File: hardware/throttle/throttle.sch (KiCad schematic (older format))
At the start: 10 parts

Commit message: Added info + revisions + date
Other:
- note added: "1.0.0"
- note added: "10/02/2021"
- note added: "Info:\nENA, IN1 and IN2 are to connect\nto the relevantly labelled pins on\nthe L298N board."
- note added: "Throttle Board"
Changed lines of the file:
@@
 Wire Wire Line
 	3400 2400 3150 2400
+Text Notes 10550 7650 0    50   ~ 0
+1.0.0
+Text Notes 8150 7650 0    50   ~ 0
+10/02/2021
+Text Notes 7350 7500 0    50   ~ 0
+Throttle Board
+Text Notes 5450 1300 0    50   ~ 0
+Info:\nENA, IN1 and IN2 are to connect\nto the relevantly labelled pins on\nthe L298N board.
 $EndSCHEMATC

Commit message: Added L298 driver
The l298n motor driver circuit has been added to the design. This is because
we need access to the sense pin. The version has also been incremented.

Signed-off-by: Computroniks <mnickson@sidingsmedia.com>
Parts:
- added C? (x2): 100nF, symbol Device:C
- added D? (x4): 1N5820, Diode_THT:D_DO-201AD_P15.24mm_Horizontal, symbol Diode:1N5820
- added J?: Screw_Terminal_01x03, symbol Connector:Screw_Terminal_01x03
- added J?: Screw_Terminal_01x02, symbol Connector:Screw_Terminal_01x02
- added Q?: BC547, Package_TO_SOT_THT:TO-92_Inline, symbol Transistor_BJT:BC547
- added R?: 330, symbol Device:R
- added R?: 1K, symbol Device:R
- added R?: 0.5, symbol Device:R
- added U?: L298HN, Package_TO_SOT_THT:TO-220-15_P2.54x2.54mm_StaggerOdd_Lead4.58mm_Vertical, symbol Driver_Motor:L298HN
- gave numbers to parts that had none: 7
- renumbered R2 to R1, R1 to R2
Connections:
- net labels added: OUT1, OUT2, SENSA, VS
- wire segments 35 -> 83
- no-connect marks 0 -> 5
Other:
- note added: "1.2.1"
- note added: "Control Circuit"
- note added: "External connections"
- note added: "Motor Driver"
- note removed: "1.0.0"
- note removed: "Info:\nENA, IN1 and IN2 are to connect\nto the relevantly labelled pins on\nthe L298N board."
- moved on the sheet: D1, D2, R1, R2, R3, R4, RV1, SW1, SW2, U1

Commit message: Added RST connector
This allows for daisy-chaining the reset pins of all the boards together
to allow for emergency stop.

Signed-off-by: Computroniks <mnickson@sidingsmedia.com>
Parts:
- added J?: Screw_Terminal_01x02, symbol Connector:Screw_Terminal_01x02
- gave numbers to parts that had none: 13
- renumbered D2 to D1, D1 to D2, R3 to R1, R1 to R2, R2 to R5, R4 to R6
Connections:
- net labels added: RST
- wire segments 83 -> 88
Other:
- note added: "1.2.2"
- note removed: "1.2.1"

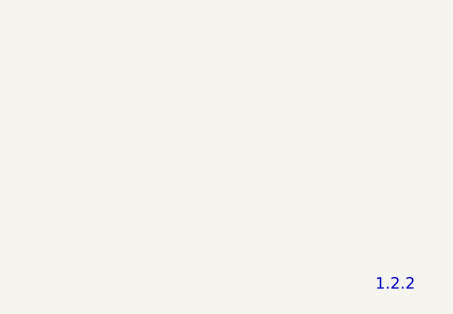
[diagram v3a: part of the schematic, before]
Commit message: Annotated symbols
Signed-off-by: Computroniks <mnickson@sidingsmedia.com>
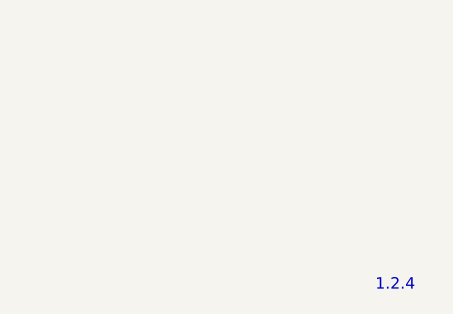
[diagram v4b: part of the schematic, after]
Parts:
- gave numbers to parts that had none: 1
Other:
- note added: "1.2.4"
- note removed: "1.2.2"
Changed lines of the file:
@@
 $EndDescr
 Text Notes 10550 7650 0    50   ~ 0
-1.2.2
+1.2.4
 Text Notes 8150 7650 0    50   ~ 0
 10/02/2021
@@
 	2900 2750 2600 2750
 $Comp
-L Connector:Screw_Terminal_01x02 J?
+L Connector:Screw_Terminal_01x02 J3
 U 1 1 602CAD0F
 P 3600 4500
-F 0 "J?" H 3680 4492 50  0000 L CNN
+F 0 "J3" H 3680 4492 50  0000 L CNN
 F 1 "Screw_Terminal_01x02" H 3680 4401 50  0000 L CNN
 F 2 "" H 3600 4500 50  0001 C CNN
